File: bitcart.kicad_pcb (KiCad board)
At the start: 4 copper layers, 136.6 x 54.6 mm, 34 parts, among them J1 Conn_01x03, J11 USB_OTG, J17 Molex 470531000, J2 Conn_02x07_Odd_Even, J3 Conn_01x03, Q1 Si7450DP, U1 MP8008, U10 MagJack-A70-112-331N126, U11 EMC2301-1-ACZL-TR, U12 MDT320M01001, U2 LTV-817S, U3 750310744, U4 TPD4EUSB30, U5 74LVC1G07SE-7, U6 TL432DBZ, U7 TPD4EUSB30, U8 TPD4EUSB30, U9 74LVC1G07SE-7

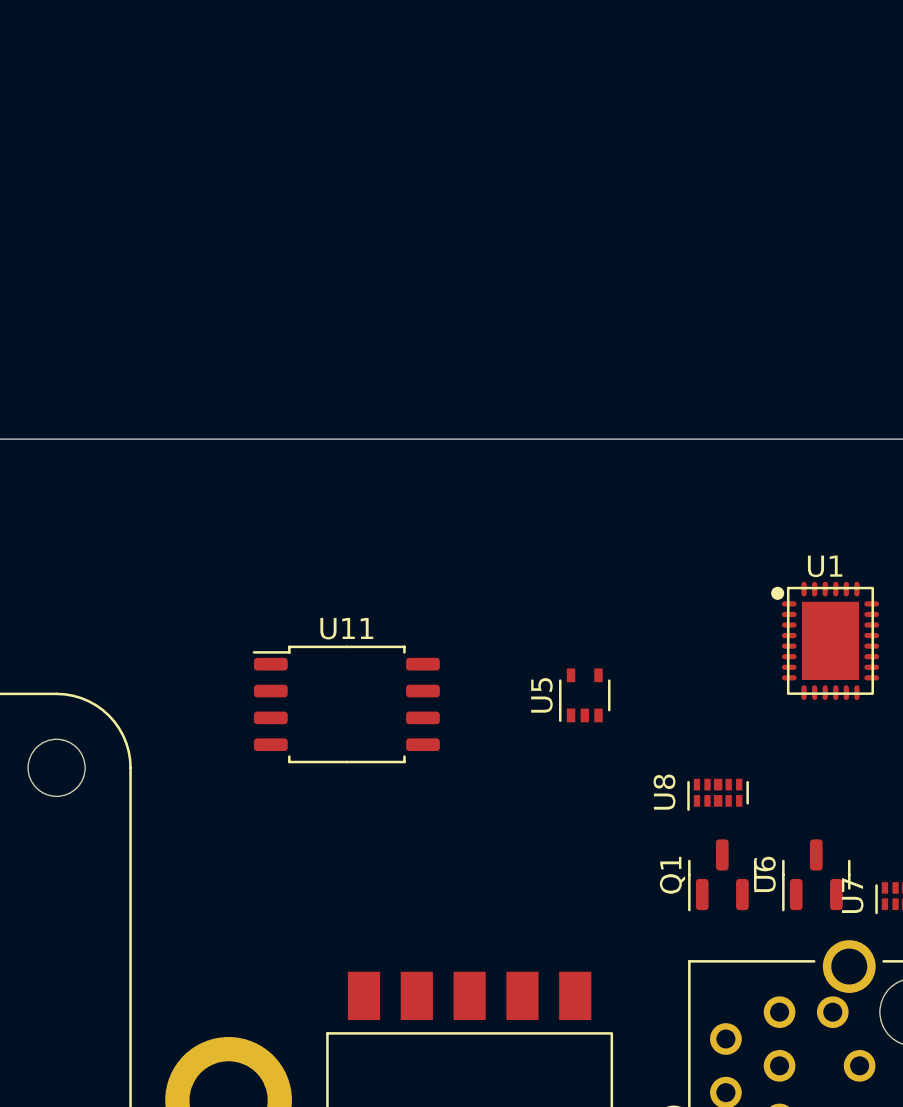
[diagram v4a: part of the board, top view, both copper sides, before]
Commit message: added flyback mosfet footprint
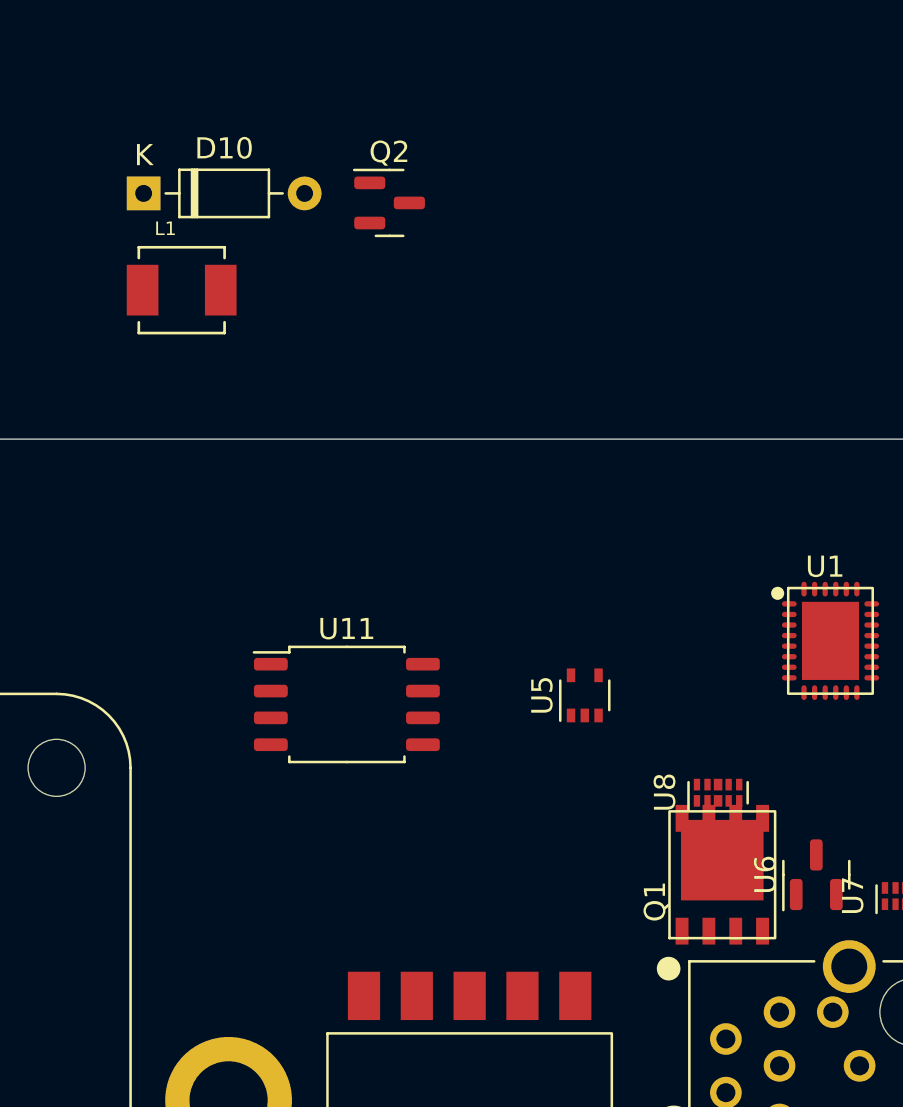
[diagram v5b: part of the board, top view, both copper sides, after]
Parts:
- added D10: 1N4148, Diode_THT:D_DO-35_SOD27_P7.62mm_Horizontal, F.Cu at (131.9, 186.0)
- added L1: 0.1uH, bitcart:IND_744373240010, F.Cu at (133.7, 190.6)
- added Q2: MMBTA06LT1G, Package_TO_SOT_SMD:SOT-23, F.Cu at (143.5, 186.4)
- Q1: value Si7450DP -> SI7430DP; footprint Package_TO_SOT_SMD:SOT-23 -> bitcart:SI7430DP
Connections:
- Q1 pad 1: Net-(D5-Pad2) -> Net-(R12-Pad1)
- Q1 pad 2: Net-(Q1-Pad2) -> Net-(R12-Pad1)
- Q1 pad 3: /PoE/W1 -> Net-(R12-Pad1)
- U1 pad 1: Net-(C1-Pad1) -> /PoE/VDD
- U1 pad 3: Net-(C1-Pad1) -> /PoE/VDD

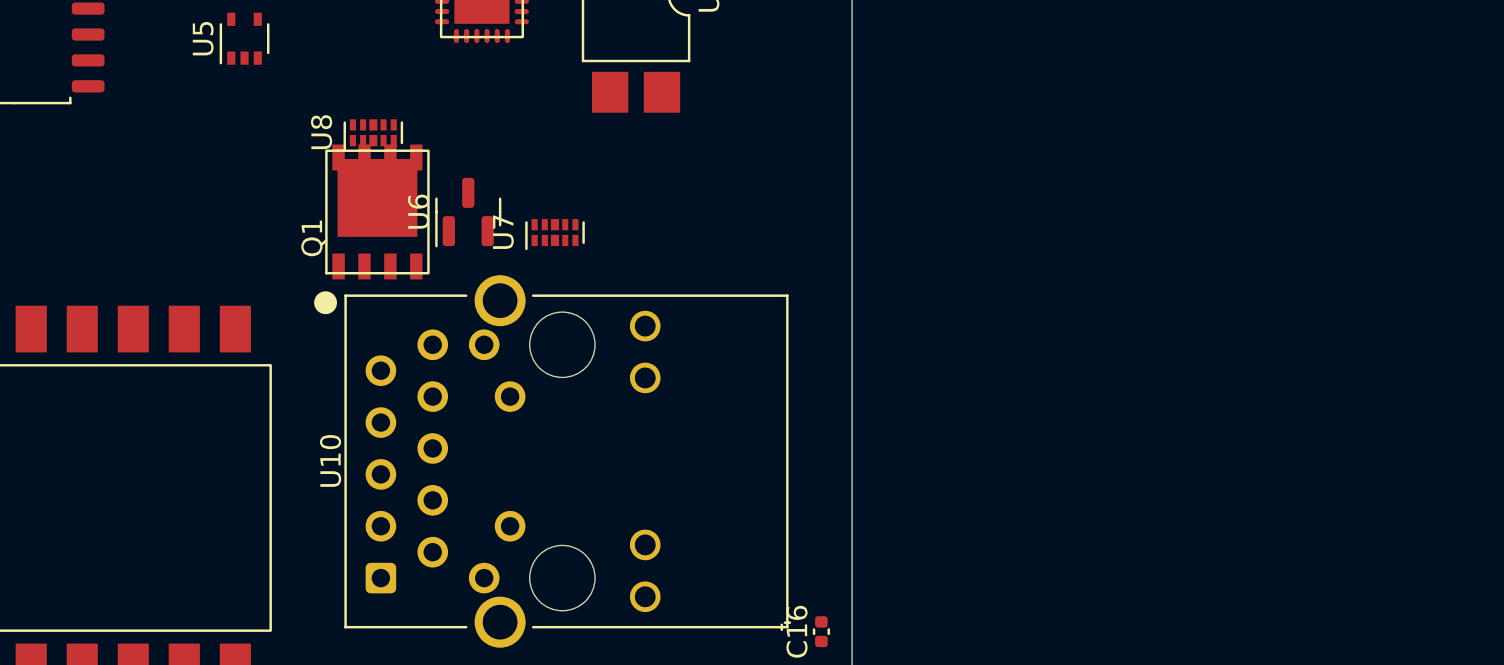
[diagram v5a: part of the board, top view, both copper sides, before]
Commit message: added a bunch more PoE footprints
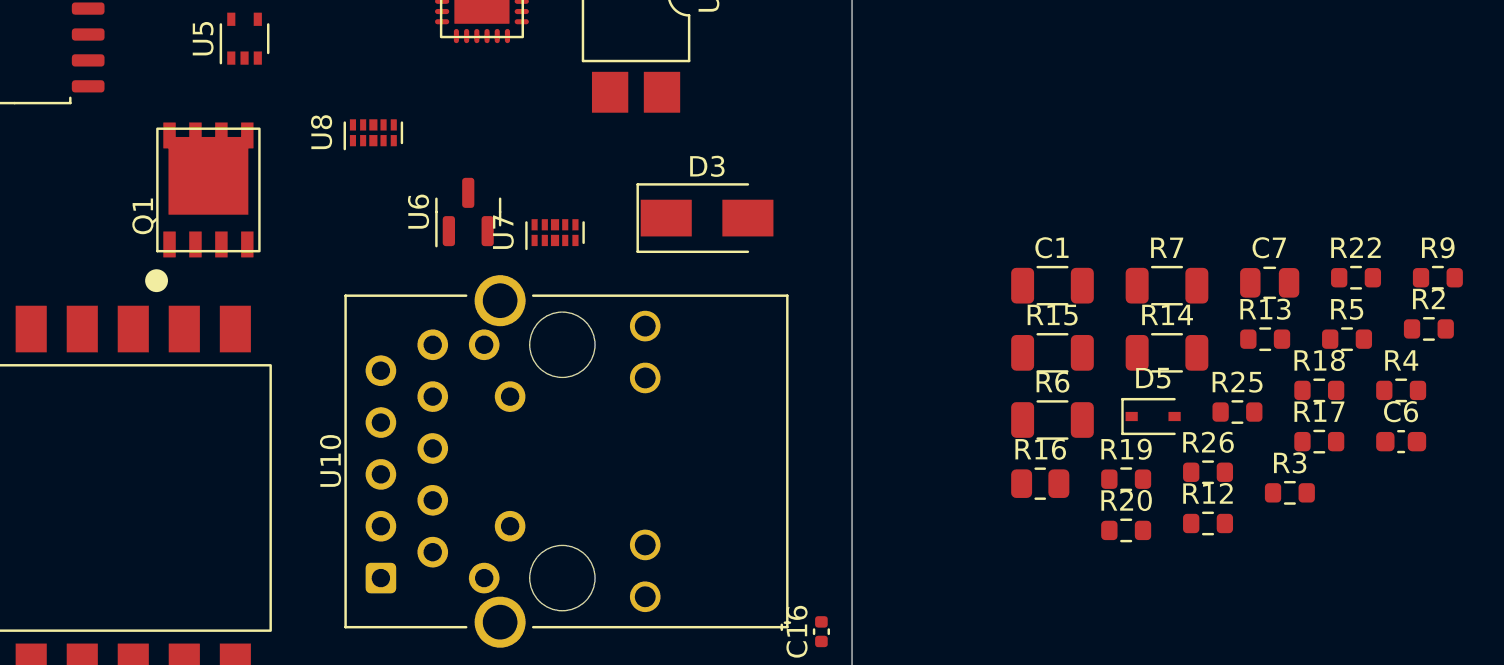
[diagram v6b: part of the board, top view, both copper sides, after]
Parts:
- added C1: 0.1uF, 100V, Resistor_SMD:R_1206_3216Metric, F.Cu at (192.4, 221.9)
- added C6: 0.22uF, Capacitor_SMD:C_0603_1608Metric, F.Cu at (209.4, 229.5)
- added C7: 4.7uF, Capacitor_SMD:C_0805_2012Metric, F.Cu at (203.0, 221.7)
- added D3: SMAJ58A, Diode_SMD:D_SMA, F.Cu at (175.4, 218.6)
- added D5: 1N4148WS, Diode_SMD:D_SOD-323, F.Cu at (197.3, 228.3)
- added R12: 4.99, Resistor_SMD:R_0603_1608Metric, F.Cu at (200.0, 233.5)
- added R13: 10k, Resistor_SMD:R_0603_1608Metric, F.Cu at (202.8, 224.5)
- added R14: 0.082, Resistor_SMD:R_1206_3216Metric, F.Cu at (198.0, 225.2)
- added R15: 0.082, Resistor_SMD:R_1206_3216Metric, F.Cu at (192.4, 225.2)
- added R16: 20, Resistor_SMD:R_0805_2012Metric, F.Cu at (191.8, 231.6)
- added R17: 2k, Resistor_SMD:R_0603_1608Metric, F.Cu at (205.4, 229.5)
- added R18: 6.8k, Resistor_SMD:R_0603_1608Metric, F.Cu at (205.4, 227.0)
- added R19: 49.9k, Resistor_SMD:R_0603_1608Metric, F.Cu at (196.0, 231.3)
- added R2: 28.7, Resistor_SMD:R_0603_1608Metric, F.Cu at (210.8, 224.0)
- added R20: 10, Resistor_SMD:R_0603_1608Metric, F.Cu at (196.0, 233.8)
- added R22: 1k, Resistor_SMD:R_0603_1608Metric, F.Cu at (207.2, 221.5)
- added R25: 191k, Resistor_SMD:R_0603_1608Metric, F.Cu at (201.4, 228.1)
- added R26: 191k, Resistor_SMD:R_0603_1608Metric, F.Cu at (200.0, 231.0)
- added R3: 24.9k, Resistor_SMD:R_0603_1608Metric, F.Cu at (204.0, 232.0)
- added R4: 9.31k, Resistor_SMD:R_0603_1608Metric, F.Cu at (209.4, 227.0)
- added R5: 100k, Resistor_SMD:R_0603_1608Metric, F.Cu at (206.8, 224.5)
- added R6: 20k, Resistor_SMD:R_1206_3216Metric, F.Cu at (192.4, 228.4)
- added R7: 20k, Resistor_SMD:R_1206_3216Metric, F.Cu at (198.0, 221.9)
- added R9: 4.99, Resistor_SMD:R_0603_1608Metric, F.Cu at (211.2, 221.5)
- moved Q1 8.35 mm to (151.0, 217.2)

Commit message: all footprints added?!
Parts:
- removed D10: 1N4148, Diode_THT:D_DO-35_SOD27_P7.62mm_Horizontal
- added C10: 0.1uF, Capacitor_SMD:C_0603_1608Metric, F.Cu at (227.6, 248.4)
- added C11: 220pF, Capacitor_SMD:C_0603_1608Metric, F.Cu at (239.8, 239.2)
- added C12: 22uF, Capacitor_SMD:C_1210_3225Metric, F.Cu at (222.7, 251.2)
- added C13: 680pF, Capacitor_SMD:C_0603_1608Metric, F.Cu at (234.3, 243.2)
- added C14: 220uF, Capacitor_SMD:CP_Elec_8x10.5, F.Cu at (213.2, 250.8)
- added C15: 0.1uF, Capacitor_SMD:C_0603_1608Metric, F.Cu at (221.8, 254.6)
- added C17: 1nF, 2000V, Capacitor_SMD:C_1812_4532Metric, F.Cu at (230.2, 236.2)
- added C18: 1uF, Capacitor_SMD:C_0603_1608Metric, F.Cu at (233.2, 245.7)
- added C2: 47uF, Capacitor_SMD:CP_Elec_10x10.5, F.Cu at (213.9, 239.7)
- added C3: 2.2uF, Capacitor_SMD:C_1210_3225Metric, F.Cu at (236.6, 235.8)
- added C4: 2.2uF, Capacitor_SMD:C_1210_3225Metric, F.Cu at (229.5, 240.8)
- added C5: 0.1uF, Capacitor_SMD:C_0805_2012Metric, F.Cu at (223.3, 243.9)
- added C8: 0.47nF, Capacitor_SMD:C_0603_1608Metric, F.Cu at (227.5, 250.9)
- added C9: 22uF, Capacitor_SMD:C_1210_3225Metric, F.Cu at (228.4, 245.0)
- added D11: 1N4148WS, Diode_SMD:D_SOD-323, F.Cu at (241.5, 235.2)
- added D4: BAV21, Diode_SMD:D_SOD-123F, F.Cu at (235.1, 240.3)
- added D6: SBR8U60P5-13, bitcart:SBR8U60P5-13, F.Cu at (223.9, 238.1)
- added D9: 9.1V, Diode_SMD:D_SOD-123, F.Cu at (222.7, 247.4)
- U2: value LTV-817S -> FOD817S
- moved U7 4.67 mm to (166.9, 214.7)
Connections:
- U1 pad 14: (no net) -> unconnected-(U1-Pad14)
- U1 pad 15: (no net) -> unconnected-(U1-Pad15)
- U1 pad 16: (no net) -> unconnected-(U1-Pad16)
- U1 pad 17: (no net) -> unconnected-(U1-Pad17)
- U1 pad 22: (no net) -> unconnected-(U1-Pad22)
- U1 pad 28: (no net) -> unconnected-(U1-Pad28)
- U1 pad 29: (no net) -> /PoE/GND1
- U1 pad 4: (no net) -> unconnected-(U1-Pad4)
- U3 pad 4: (no net) -> unconnected-(U3-Pad4)
- U3 pad 8: (no net) -> unconnected-(U3-Pad8)
